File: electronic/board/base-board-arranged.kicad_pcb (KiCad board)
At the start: 2 copper layers, 272 x 164 mm, 112 parts, among them P1 BEAGLEBONE_BLACK, P100_0 CONN_02X10, P100_1 CONN_02X10, P100_10 CONN_02X10, P100_11 CONN_02X10, P100_12 CONN_02X10, P100_13 CONN_02X10, P100_14 CONN_02X10, P100_15 CONN_02X10, P100_16 CONN_02X10, P100_17 CONN_02X10, P100_2 CONN_02X10, P100_3 CONN_02X10, P100_4 CONN_02X10, P100_5 CONN_02X10, P100_6 CONN_02X10, P100_7 CONN_02X10, P100_8 CONN_02X10, P100_9 CONN_02X10, P2 I2C, P3 PWR, P5 CONN_02X10, P6 CONN_02X10

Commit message: Some hw, +others
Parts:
- added Q1: IRF540N, TO-220, F.Cu at (297.6, 151.7)
- added R2: 1k, Resistors_ThroughHole:Resistor_Ceramic_Horizontal_L50mm-W14mm-H13mm-p60mm, F.Cu at (295.1, 116.5)
- R100_16: footprint w_pth_resistors:R25x8 -> Resistors_ThroughHole:Resistor_Ceramic_Horizontal_L50mm-W14mm-H13mm-p60mm
- moved R100_16 11.1 mm to (306.9, 161.7)
- moved R103_5 0.98 mm to (193.7, 88.4)
- moved R102_5 0.74 mm to (191.1, 88.4)
- moved R100_5 0.62 mm to (185.9, 88.4)
- moved R101_5 0.37 mm to (188.4, 88.4)
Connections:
- B4 pad 2: /GND3 -> Net-(B4-Pad2)
- P1 pad A1: /GND -> /GND2
- P1 pad A2: /GND -> /GND2
- P1 pad B1: /GND -> /GND1
- P1 pad B2: /GND -> /GND1
- P3 pad 2: /GND -> /GND1
- P5 pad 1: /GND -> Net-(P5-Pad1)
- P5 pad 2: /GND -> Net-(P5-Pad1)
- P6 pad 1: /GND -> /GND1
- P6 pad 2: /GND -> /GND1
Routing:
- net /GND: track 834.7 -> 0.00 mm
- net /VDD_5V_DOWN: track 415.6 -> 0.00 mm
- net /12V+: track 359.2 -> 0.00 mm
- net /GND12V: track 339.5 -> 0.00 mm
- net /DC_3.3V: track 320.1 -> 0.00 mm
- net /GPIO0_30: track 260.4 -> 0.00 mm
- net /VDD_5V_TOP: track 257.4 -> 0.00 mm
- net /GPIO0_31: track 255.9 -> 0.00 mm
- net /GPIO1_16: track 252.1 -> 0.00 mm
- net /GPIO1_4: track 237.0 -> 0.00 mm
- net /GPIO1_0: track 235.6 -> 0.00 mm
- net /GPIO2_22: track 234.2 -> 0.00 mm
- net /GPIO2_23: track 232.8 -> 0.00 mm
- net /GPIO1_28: track 231.7 -> 0.00 mm
- net /GPIO0_10: track 231.6 -> 0.00 mm
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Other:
- outline, holes or cut-outs redrawn
- board text added: "Main Board - 08/2016"
- board text removed: "Main Board - 08/2015"

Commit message: Main Board
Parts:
- removed R103_15: 1K, w_pth_resistors:RC03
- added R3: 47k, w_pth_resistors:RC03, F.Cu at (289.2, 187.8)
- B3, B4: footprint w_pth_resistors:RC05 -> w_pth_resistors:RC07
- Q1: footprint TO-220 -> Transistors_TO-220:TO-220_Neutral123_Horizontal_LargePads
- R100_10, R100_11, R100_12, R100_13, R100_15, R100_4, R100_5, R100_6, R100_7, R100_9, R101_10, R101_11, R101_12, R101_15, R101_4, R101_5, R101_6, R101_7, R101_9, R102_10, R102_11, R102_12, R102_4, R102_5, R102_6, R102_7, R102_9, R103_10, R103_11, R103_12, R103_4, R103_5, R103_6, R103_7, R103_9: footprint w_pth_resistors:RC03 -> w_pth_resistors:RC07
- R100_16: footprint Resistors_ThroughHole:Resistor_Ceramic_Horizontal_L50mm-W14mm-H13mm-p60mm -> w_pth_resistors:R25x8
- R100_3, R101_3, R102_3: footprint w_pth_resistors:RC03 -> w_pth_resistors:RC05
- R2: value 1k -> 10k; footprint Resistors_ThroughHole:Resistor_Ceramic_Horizontal_L50mm-W14mm-H13mm-p60mm -> w_pth_resistors:RC07
- moved R2 80.0 mm to (282.0, 195.4), turned to 270 degrees
- moved Q1 32.6 mm to (289.6, 183.3)
- moved R100_14 10.8 mm to (192.9, 191.3)
- moved R101_14 10.4 mm to (190.6, 192.6)
- moved R102_14 9.25 mm to (188.1, 194.2)
- moved R102_15 8.36 mm to (213.5, 192.1)
- moved R103_14 7.89 mm to (185.7, 195.6)
- moved R100_16 7.42 mm to (309.7, 154.9)
- moved R100_2 6.96 mm to (132.2, 105.1)
- moved R100_3 6.67 mm to (152.7, 106.1)
- moved R102_1 6.49 mm to (103.9, 110.8)
- moved R101_2 6.06 mm to (129.0, 107.3)
- moved R103_1 6.02 mm to (100.9, 113.4)
- moved R102_2 5.56 mm to (125.8, 109.8)
- moved R103_2 5.48 mm to (122.9, 112.8)
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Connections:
- R2 pad 2: /SYS_RESETn -> /GPIO3_15
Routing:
- net /GND: track 0.00 -> 425.8 mm
- net /VDD_5V_DOWN: track 0.00 -> 354.5 mm
- net /12V+: track 0.00 -> 334.3 mm
- net /GND12V: track 0.00 -> 325.8 mm
- net /DC_3.3V: track 0.00 -> 316.0 mm
- net /GPIO0_30: track 0.00 -> 273.6 mm
- net /GPIO0_31: track 0.00 -> 267.3 mm
- net /GPIO1_16: track 0.00 -> 262.8 mm
- net /GPIO0_5: track 0.00 -> 240.7 mm
- net /GPIO1_4: track 0.00 -> 234.7 mm
- net /GPIO1_0: track 0.00 -> 233.3 mm
- net /GPIO2_22: track 0.00 -> 232.0 mm
- net /GPIO2_23: track 0.00 -> 230.6 mm
- net /GPIO1_28: track 0.00 -> 229.4 mm
- net /GPIO1_15: track 0.00 -> 229.2 mm
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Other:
- rule trace_min: 0.4 -> 0.2

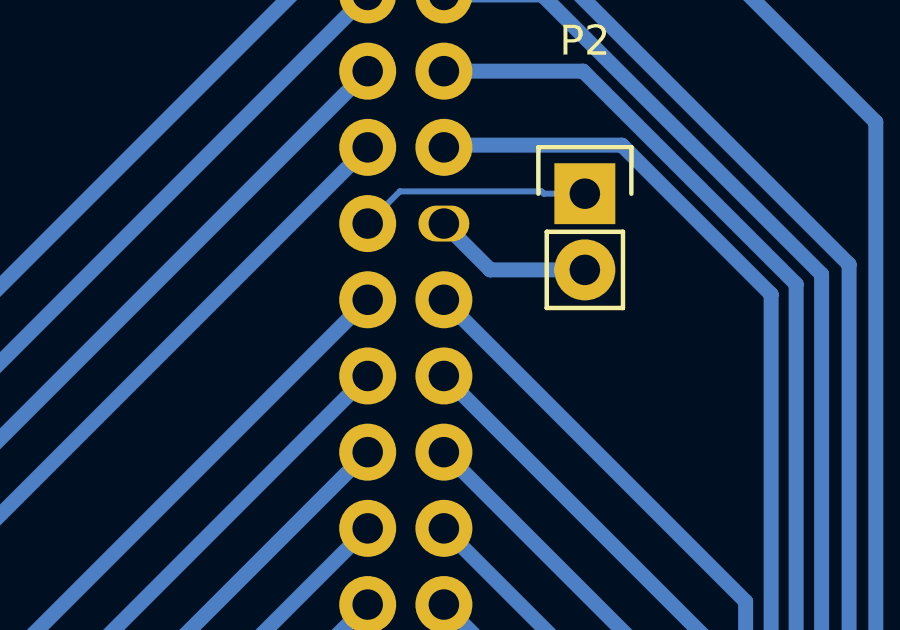
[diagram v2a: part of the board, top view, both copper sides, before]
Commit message: Main board, IOs gated
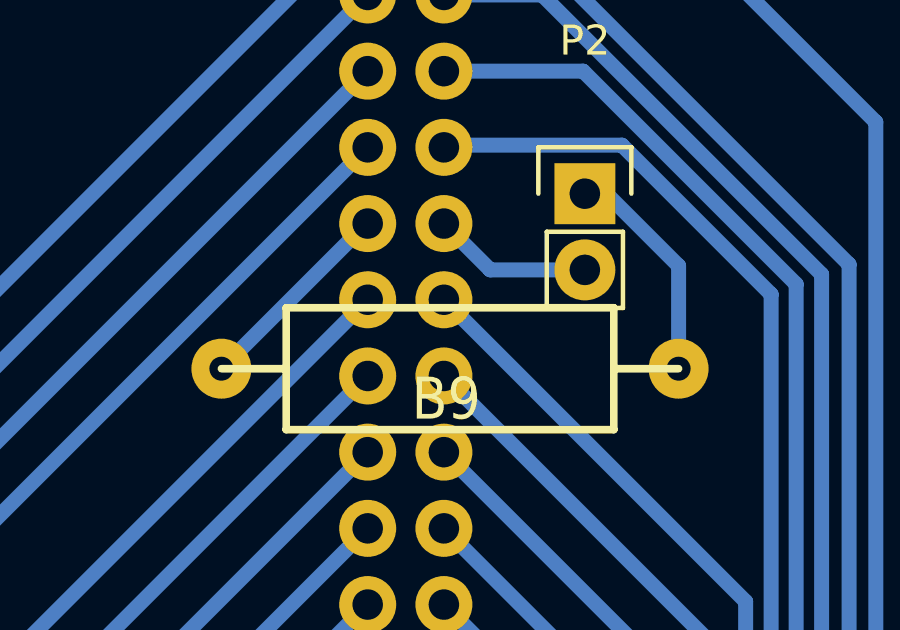
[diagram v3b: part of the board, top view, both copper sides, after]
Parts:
- added B9: 0, w_pth_resistors:RC07, F.Cu at (313.2, 103.5)
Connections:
- P2 pad 1: /I2C2_SDA -> Net-(B9-Pad1)
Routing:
- net Net-(B9-Pad1): track 0.00 -> 7.55 mm
- net /I2C2_SDA: track 7.71 -> 6.88 mm
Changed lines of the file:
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@@
 (kicad_pcb (version 4) (host pcbnew "(2015-07-19 BZR 5960)-product")
   (general
-    (links 456)
+    (links 457)
     (no_connects 0)
-    (area 63.6422 54.925 336.602201 225.721601)
+    (area 64.122559 56.150039 336.210841 220.237521)
     (thickness 1.6)
     (drawings 13)
-    (tracks 1011)
+    (tracks 1012)
     (zones 0)
-    (modules 114)
-    (nets 192)
+    (modules 115)
+    (nets 193)
   )
   (page A3)
@@
     (mod_text_size 1 1)
     (mod_text_width 0.15)
-    (pad_size 1.2 1.7)
+    (pad_size 1.9 1.9)
     (pad_drill 1.016)
     (pad_to_mask_clearance 0)
@@
   (net 190 "Net-(Q1-Pad1)")
   (net 191 "Net-(P5-Pad1)")
+  (net 192 "Net-(B9-Pad1)")
   (net_class Default "This is the default net class."
     (clearance 0.33)
@@
     (add_net "Net-(B4-Pad2)")
     (add_net "Net-(B7-Pad1)")
+    (add_net "Net-(B9-Pad1)")
     (add_net "Net-(P100_0-Pad11)")
     (add_net "Net-(P100_0-Pad13)")
@@
     (pad B18 thru_hole circle (at 40.005 4.445 270) (size 1.9 1.9) (drill 1.016) (layers *.Cu *.Mask B.SilkS)
       (net 58 /GPIO0_4))
-    (pad B19 thru_hole oval (at 42.545 1.905 270) (size 1.2 1.7) (drill 1.016) (layers *.Cu *.Mask B.SilkS)
+    (pad B19 thru_hole circle (at 42.545 1.905 270) (size 1.9 1.9) (drill 1.016) (layers *.Cu *.Mask B.SilkS)
       (net 169 /I2C2_SCL))
     (pad B20 thru_hole circle (at 42.545 4.445 270) (size 1.9 1.9) (drill 1.016) (layers *.Cu *.Mask B.SilkS)
@@
     (fp_line (start -1.27 3.81) (end 1.27 3.81) (layer F.SilkS) (width 0.15))
     (pad 1 thru_hole rect (at 0 0) (size 2.032 2.032) (drill 1.016) (layers *.Cu *.Mask F.SilkS)
-      (net 170 /I2C2_SDA))
+      (net 192 "Net-(B9-Pad1)"))
     (pad 2 thru_hole oval (at 0 2.54) (size 2.032 2.032) (drill 1.016) (layers *.Cu *.Mask F.SilkS)
       (net 169 /I2C2_SCL))
@@
     )
   )
+  (module w_pth_resistors:RC07 (layer F.Cu)
+    (at 313.1636 103.461 180)
+    (descr "Resistor, RC07")
+    (tags R)
+    (autoplace_cost180 10)
+    (fp_text reference B9 (at 0.127 -1.016 180) (layer F.SilkS)
+      (effects (font (size 1.397 1.27) (thickness 0.2032)))
+    )
+    (fp_text value 0 (at 0 1.016 180) (layer F.SilkS) hide
+      (effects (font (size 1.397 1.27) (thickness 0.2032)))
+    )
+    (fp_line (start -5.461 0) (end -5.461 -2.032) (layer F.SilkS) (width 0.254))
+    (fp_line (start -5.461 -2.032) (end 5.461 -2.032) (layer F.SilkS) (width 0.254))
+    (fp_line (start 5.461 -2.032) (end 5.461 2.032) (layer F.SilkS) (width 0.254))
+    (fp_line (start 5.461 2.032) (end -5.461 2.032) (layer F.SilkS) (width 0.254))
+    (fp_line (start -5.461 2.032) (end -5.461 0) (layer F.SilkS) (width 0.254))
+    (fp_line (start 5.461 0) (end 7.62 0) (layer F.SilkS) (width 0.254))
+    (fp_line (start -7.62 0) (end -5.461 0) (layer F.SilkS) (width 0.254))
+    (pad 1 thru_hole circle (at -7.62 0 180) (size 1.99898 1.99898) (drill 0.8001) (layers *.Cu *.Mask F.SilkS)
+      (net 192 "Net-(B9-Pad1)"))
+    (pad 2 thru_hole circle (at 7.62 0 180) (size 1.99898 1.99898) (drill 0.8001) (layers *.Cu *.Mask F.SilkS)
+      (net 170 /I2C2_SDA))
+    (model walter/pth_resistors/rc07.wrl
+      (at (xyz 0 0 0))
+      (scale (xyz 1 1 1))
+      (rotate (xyz 0 0 0))
+    )
+  )
   (gr_line (start 276.0886 76.461) (end 276.0886 76.461) (angle 90) (layer Edge.Cuts) (width 0.1))
   (gr_line (start 276.0886 56.211) (end 276.0886 76.461) (angle 90) (layer Edge.Cuts) (width 0.1))
@@
   (segment (start 314.5043 100.1674) (end 312.96 98.6231) (width 0.5) (layer B.Cu) (net 169))
   (segment (start 317.659 100.1674) (end 314.5043 100.1674) (width 0.5) (layer B.Cu) (net 169))
-  (segment (start 311.4916 97.5515) (end 310.42 98.6231) (width 0.2) (layer B.Cu) (net 170))
-  (segment (start 316.2171 97.5515) (end 311.4916 97.5515) (width 0.2) (layer B.Cu) (net 170))
-  (segment (start 316.293 97.6274) (end 316.2171 97.5515) (width 0.2) (layer B.Cu) (net 170))
-  (segment (start 317.659 97.6274) (end 316.293 97.6274) (width 0.2) (layer B.Cu) (net 170))
+  (segment (start 310.42 98.6231) (end 310.3815 98.6231) (width 0.5) (layer B.Cu) (net 170))
+  (segment (start 310.3815 98.6231) (end 305.5436 103.461) (width 0.5) (layer B.Cu) (net 170))
   (segment (start 132.5175 94.2975) (end 134.4987 96.2787) (width 0.5) (layer B.Cu) (net 171))
   (segment (start 122.24 94.2975) (end 132.5175 94.2975) (width 0.5) (layer B.Cu) (net 171))
@@
   (segment (start 285.429 187.786) (end 281.994 187.786) (width 0.5) (layer B.Cu) (net 190))
   (segment (start 266.39 165.4) (end 263.85 165.4) (width 0.5) (layer B.Cu) (net 191))
+  (segment (start 317.659 97.6274) (end 318.38 97.6274) (width 0.5) (layer B.Cu) (net 192))
+  (segment (start 318.38 97.6274) (end 320.7836 100.031) (width 0.5) (layer B.Cu) (net 192))
+  (segment (start 320.7836 100.031) (end 320.7836 103.461) (width 0.5) (layer B.Cu) (net 192))
   (zone (net 0) (net_name "") (layer B.Cu) (hatch edge 0.508)
     (connect_pads (clearance 0.508))
